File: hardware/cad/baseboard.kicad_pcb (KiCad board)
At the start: 6 copper layers, 100 x 65 mm, 129 parts, among them J201 1/4" JACK, STEREO, J202 1/4" JACK, STEREO, J301 FFC CONNECTOR, J303 2x2 PIN HEADER, J306 6-440054-2, J308 6-440054-2, J310 6-440054-2, J311 6-440054-2, J401 DC POWER JACK, J402 6-440054-2, Q301 DMN2050, Q302 DMN2050, U201 OPA1679, U202 OPA1679, U301 STM32G031K8U6, U302 ADG5434, U401 LM337, U402 LM317, U403 ADP5070, U404 LM317

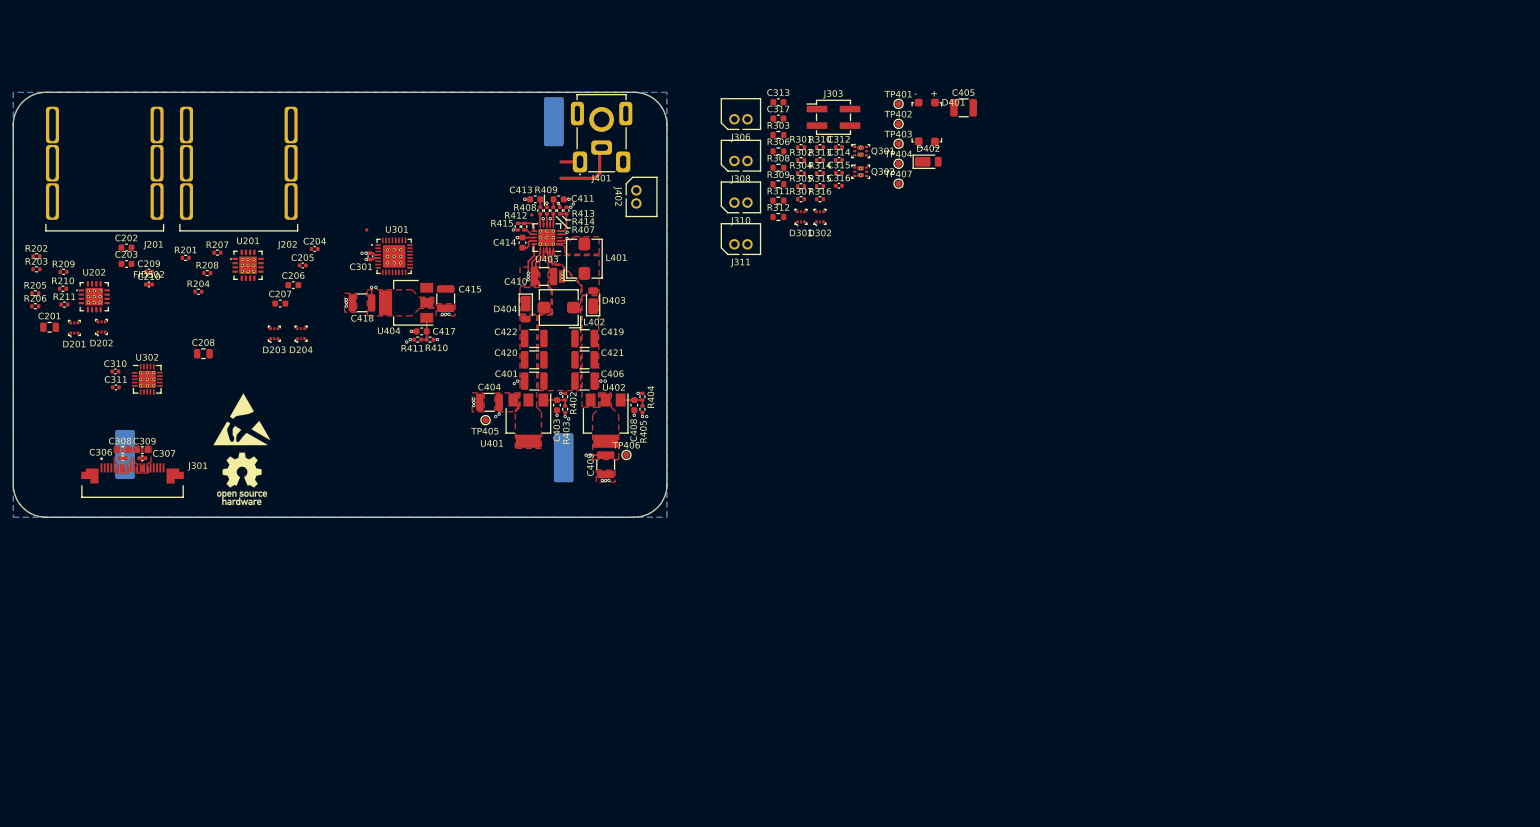
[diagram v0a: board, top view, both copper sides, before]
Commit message: finalized schematic
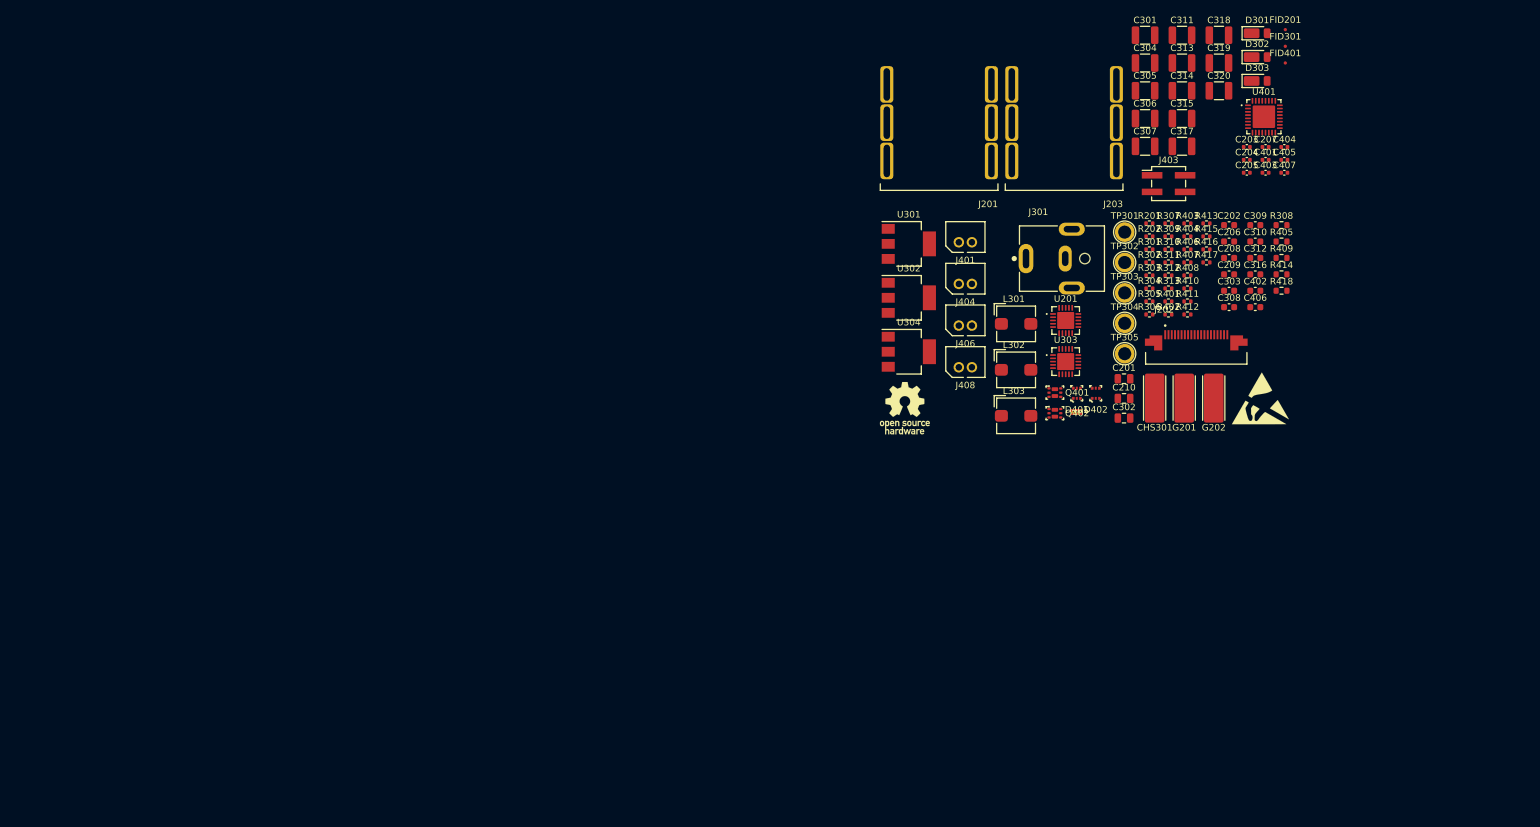
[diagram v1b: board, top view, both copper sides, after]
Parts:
- removed C408, C414, C417: 2.2µ, Capacitor_SMD:C_0603_1608Metric
- removed C409, C410, C415, C418, C419, C420, C421, C422: 22µ, Capacitor_SMD:C_1210_3225Metric
- removed C411: 2n, Capacitor_SMD:C_0603_1608Metric
- removed C413: 39n, Capacitor_SMD:C_0603_1608Metric
- removed CHS401, CHS501, CHS502: Chassis, Library:Harwin_EMI_Finger_S7061-46R
- removed D201, D202, D203, D204: RSB10JS2, Library:RSB12JS2
- removed D403, D404: DFLS240L-7, Library:D_PowerDI-123_THERMAL_PAD
- removed FID501, FID502, FID503: Fiducial, Fiducial:Fiducial_0.5mm_Mask1mm
- removed G501: OSHW LOGO, Symbol:OSHW-Logo_7.5x8mm_SilkScreen
- removed G502: ESD SYMBOL, Symbol:ESD-Logo_8.9x8mm_SilkScreen
- removed J303: 2x2 PIN HEADER, Connector_PinHeader_2.54mm:PinHeader_2x02_P2.54mm_Vertical_SMD
- removed J306, J308, J310, J311, J402: 6-440054-2, Library:TE_HPI_2.0MM_PITCH_MALE_HEADER_2POS
- removed L401, L402: 22µ, Inductor_SMD:L_Bourns_SRP5030T
- removed NT401: NetTie_2, Library:Net_Tie
- removed Q301, Q302: DMN2050, Library:DMN2050LFDB_THERMAL_VIAS
- removed R203: 1M, Resistor_SMD:R_0402_1005Metric
- removed R204, R205, R206, R207, R208, R209, R210, R211: 49.9k, Resistor_SMD:R_0402_1005Metric
- removed R314: 1k, Resistor_SMD:R_0402_1005Metric
- removed R315, R316: 120R, Resistor_SMD:R_0402_1005Metric
- removed TP401, TP402, TP403, TP404, TP405, TP406, TP407: TestPoint, TestPoint:TestPoint_Pad_D1.0mm
- removed U202: OPA1679, Library:OPA1679
- removed U402, U404: LM317, Package_TO_SOT_SMD:SOT-223-3_TabPin2
- removed U403: ADP5070, Library:LFCSP-20-1EP_4x4mm_P0.5mm_EP2.6x2.6mm_ThermalVias
- added C302: 150pF, Capacitor_SMD:C_0805_2012Metric, F.Cu at (211.4, 103.1)
- added C303: 2.2µF, Capacitor_SMD:C_0603_1608Metric, F.Cu at (227.5, 83.7)
- added C304: 10µF, Capacitor_SMD:C_1210_3225Metric, F.Cu at (214.6, 48.8)
- added C305: 10µF, Capacitor_SMD:C_1210_3225Metric, F.Cu at (214.6, 53.1)
- added C318: 10µF, Capacitor_SMD:C_1210_3225Metric, F.Cu at (225.9, 44.6)
- added C319: 10µF, Capacitor_SMD:C_1210_3225Metric, F.Cu at (225.9, 48.8)
- added C320: 10µF, Capacitor_SMD:C_1210_3225Metric, F.Cu at (225.9, 53.1)
- added C402: 2.2µF, Capacitor_SMD:C_0603_1608Metric, F.Cu at (231.5, 83.7)
- added C407: 100nF, Capacitor_SMD:C_0402_1005Metric, F.Cu at (235.9, 65.6)
- added CHS301: CHASSIS, Library:Harwin_EMI_Finger_S7061-46R, F.Cu at (216.1, 100.1)
- added D303: DFLS240L-7, Library:D_PowerDI-123_THERMAL_PAD, F.Cu at (231.8, 51.6)
- added FID201: FIDUCIAL, Fiducial:Fiducial_0.5mm_Mask1mm, F.Cu at (236.1, 43.7)
- added FID301: FIDUCIAL, Fiducial:Fiducial_0.5mm_Mask1mm, F.Cu at (236.1, 46.3)
- added FID401: FIDUCIAL, Fiducial:Fiducial_0.5mm_Mask1mm, F.Cu at (236.1, 48.8)
- added G101: OSHW LOGO, Symbol:OSHW-Logo_7.5x8mm_SilkScreen, F.Cu at (177.9, 101.6)
- added G102: ESD SYMBOL, Symbol:ESD-Logo_8.9x8mm_SilkScreen, F.Cu at (232.3, 100.1)
- added G201: CHASSIS, Library:Harwin_EMI_Finger_S7061-46R, F.Cu at (220.6, 100.1)
- added G202: CHASSIS, Library:Harwin_EMI_Finger_S7061-46R, F.Cu at (225.1, 100.1)
- added J203: 1/4" JACK, STEREO, Library:Amphenol_ACJS-IHS, F.Cu at (202.2, 58.3)
- added J403: 2x2 PIN HEADER, Connector_PinHeader_2.54mm:PinHeader_2x02_P2.54mm_Vertical_SMD, F.Cu at (218.2, 67.3)
- added J404: 6-440054-2, Library:TE_HPI_2.0MM_PITCH_MALE_HEADER_2POS, F.Cu at (187.1, 84.4)
- added J406: 6-440054-2, Library:TE_HPI_2.0MM_PITCH_MALE_HEADER_2POS, F.Cu at (187.1, 90.7)
- added J408: 6-440054-2, Library:TE_HPI_2.0MM_PITCH_MALE_HEADER_2POS, F.Cu at (187.1, 97.1)
- added L301: 22µH, Inductor_SMD:L_Bourns_SRP5030T, F.Cu at (194.9, 88.7)
- added L302: 22µH, Inductor_SMD:L_Bourns_SRP5030T, F.Cu at (194.9, 95.8)
- added L303: 22µH, Inductor_SMD:L_Bourns_SRP5030T, F.Cu at (194.9, 102.8)
- added NT301: NET TIE, Library:Net_Tie, F.Cu at (204.2, 102.2)
- added Q401: DMN2050, Library:DMN2050LFDB, F.Cu at (200.8, 99.2)
- added Q402: DMN2050, Library:DMN2050LFDB, F.Cu at (200.8, 102.4)
- added R401: 120Ω, Resistor_SMD:R_0402_1005Metric, F.Cu at (218.2, 85.3)
- added R406: 120Ω, Resistor_SMD:R_0402_1005Metric, F.Cu at (221.1, 77.3)
- added R416: 120Ω, Resistor_SMD:R_0402_1005Metric, F.Cu at (224.0, 77.3)
- added R417: 750Ω, Resistor_SMD:R_0402_1005Metric, F.Cu at (224.0, 79.3)
- added R418: 15Ω, Resistor_SMD:R_0603_1608Metric, F.Cu at (235.5, 83.7)
- added TP301: TEST POINT, TestPoint:TestPoint_Plated_Hole_D2.0mm, F.Cu at (211.5, 74.7)
- added TP302: TEST POINT, TestPoint:TestPoint_Plated_Hole_D2.0mm, F.Cu at (211.5, 79.3)
- added TP303: TEST POINT, TestPoint:TestPoint_Plated_Hole_D2.0mm, F.Cu at (211.5, 84.0)
- added TP304: TEST POINT, TestPoint:TestPoint_Plated_Hole_D2.0mm, F.Cu at (211.5, 88.6)
- added TP305: TEST POINT, TestPoint:TestPoint_Plated_Hole_D2.0mm, F.Cu at (211.5, 93.3)
- added U303: ADP5070, Library:LFCSP-20-1EP_4x4mm_P0.5mm_EP2.6x2.6mm, F.Cu at (202.5, 94.5)
- added U304: LM317, Package_TO_SOT_SMD:SOT-223-3_TabPin2, F.Cu at (178.5, 93.0)
- C201: value 150p -> 150pF
- C202: value 39n -> 39nF
- C203, C207: value 39n -> 100nF; footprint Capacitor_SMD:C_0603_1608Metric -> Capacitor_SMD:C_0402_1005Metric
- C204, C205: value 100n -> 100nF
- C206: value 39n -> 2.2µF
- C208: value 150p -> 2.2µF; footprint Capacitor_SMD:C_0805_2012Metric -> Capacitor_SMD:C_0603_1608Metric
- C209: value 100n -> 39nF; footprint Capacitor_SMD:C_0402_1005Metric -> Capacitor_SMD:C_0603_1608Metric
- C210: value 100n -> 150pF; footprint Capacitor_SMD:C_0402_1005Metric -> Capacitor_SMD:C_0805_2012Metric
- C301, C306, C307, C311, C314, C315: value 100n -> 10µF; footprint Capacitor_SMD:C_0402_1005Metric -> Capacitor_SMD:C_1210_3225Metric
- C308: value 2.2µ -> 58nF
- C309: value 2.2µ -> 2.2µF
- C310: value 100n -> 10nF; footprint Capacitor_SMD:C_0402_1005Metric -> Capacitor_SMD:C_0603_1608Metric
- C312, C316: value 100n -> 2.2µF; footprint Capacitor_SMD:C_0402_1005Metric -> Capacitor_SMD:C_0603_1608Metric
- C313, C317: value 2.2µ -> 10µF; footprint Capacitor_SMD:C_0603_1608Metric -> Capacitor_SMD:C_1210_3225Metric
- C401, C404, C405: value 22µ -> 100nF; footprint Capacitor_SMD:C_1210_3225Metric -> Capacitor_SMD:C_0402_1005Metric
- C403: value 2.2µ -> 100nF; footprint Capacitor_SMD:C_0603_1608Metric -> Capacitor_SMD:C_0402_1005Metric
- C406: value 22µ -> 2.2µF; footprint Capacitor_SMD:C_1210_3225Metric -> Capacitor_SMD:C_0603_1608Metric
- D301: value RSB10JS2 -> DFLZ13Q-7; footprint Library:RSB12JS2 -> Library:D_PowerDI-123_THERMAL_PAD
- D302: value RSB10JS2 -> DFLS240L-7; footprint Library:RSB12JS2 -> Library:D_PowerDI-123_THERMAL_PAD
- D401: value CD-HD2004 -> RSB10JS2; footprint Library:CD-HD2004L -> Library:RSB12JS2
- D402: value DFLZ13Q-7 -> RSB10JS2; footprint Library:D_PowerDI-123_THERMAL_PAD -> Library:RSB12JS2
- J202: value 1/4" JACK, STEREO -> FFC CONNECTOR; footprint Library:Amphenol_ACJS-IHS -> Library:AMPHENOL_SFV20R-2STE1HLF
- J301: value FFC CONNECTOR -> JACK, DC; footprint Library:AMPHENOL_SFV20R-2STE1HLF -> Library:CUI_PJ-063AH
- J401: value DC POWER JACK -> 6-440054-2; footprint Library:CUI_PJ-047 -> Library:TE_HPI_2.0MM_PITCH_MALE_HEADER_2POS
- R201, R310: value 49.9k -> 1MΩ
- R202: value 1M -> 49.9kΩ
- R301: value 120R -> 750Ω
- R302, R403: value 120R -> 120Ω
- R303: value 15R -> 750Ω; footprint Resistor_SMD:R_0603_1608Metric -> Resistor_SMD:R_0402_1005Metric
- R304: value 1k -> 33kΩ
- R305: value 49.9k -> 120Ω
- R306: value 15R -> 3.3kΩ; footprint Resistor_SMD:R_0603_1608Metric -> Resistor_SMD:R_0402_1005Metric
- R307, R313: value 1k -> 71.5kΩ
- R308: value 15R -> 200Ω
- R309: value 15R -> 62.5kΩ; footprint Resistor_SMD:R_0603_1608Metric -> Resistor_SMD:R_0402_1005Metric
- R311: value 15R -> 120Ω; footprint Resistor_SMD:R_0603_1608Metric -> Resistor_SMD:R_0402_1005Metric
- R312: value 15R -> 1MΩ; footprint Resistor_SMD:R_0603_1608Metric -> Resistor_SMD:R_0402_1005Metric
- R402: value 750R -> 49.9kΩ
- R404: value 750R -> 750Ω
- R405: value 120R -> 200Ω; footprint Resistor_SMD:R_0402_1005Metric -> Resistor_SMD:R_0603_1608Metric
- R407: value 18k -> 120Ω
- R408: value 1.8k -> 750Ω
- R409: value 100k -> 15Ω; footprint Resistor_SMD:R_0402_1005Metric -> Resistor_SMD:R_0603_1608Metric
- R410: value 200R -> 120Ω
- R411: value 120R -> 49.9kΩ
- R412: value 71.5k -> 120Ω
- R413: value 1.4M -> 750Ω
- R414: value 100k -> 200Ω; footprint Resistor_SMD:R_0402_1005Metric -> Resistor_SMD:R_0603_1608Metric
- R415: value 1.15M -> 120Ω
- U201: value OPA1679 -> ADG5434; footprint Library:OPA1679 -> Library:LFCSP-20-1EP_4x4mm_P0.5mm_EP2.6x2.6mm
- U301: value STM32G031K8U6 -> LM337; footprint Library:QFN-32-1EP_5x5mm_P0.5mm_EP3.45x3.45mm_ThermalVias -> Package_TO_SOT_SMD:SOT-223-3_TabPin2
- U302: value ADG5434 -> LM317; footprint Library:LFCSP-20-1EP_4x4mm_P0.5mm_EP2.6x2.6mm_ThermalVias -> Package_TO_SOT_SMD:SOT-223-3_TabPin2
- U401: value LM337 -> STM32G031K8U6; footprint Package_TO_SOT_SMD:SOT-223-3_TabPin2 -> Library:QFN-32-1EP_5x5mm_P0.5mm_EP3.45x3.45mm
- moved C310 175.5 mm to (231.5, 76.1)
- moved C309 173.7 mm to (231.5, 73.6), turned to 0 degrees
- moved C203 172.3 mm to (230.2, 61.7)
- moved C311 171.7 mm to (220.3, 44.6)
- moved C308 170.6 mm to (227.5, 86.2)
- moved R202 170.3 mm to (215.3, 75.3)
- moved C202 168.7 mm to (227.5, 73.6)
- moved C209 165.2 mm to (227.5, 81.1)
- moved C306 164.8 mm to (214.6, 57.3)
- moved C201 164.5 mm to (211.4, 97.1)
- moved C307 160.6 mm to (214.6, 61.6), turned to 0 degrees
- moved C208 157.6 mm to (227.5, 78.6)
- moved C207 152.6 mm to (233.1, 61.7)
- moved C210 150.2 mm to (211.4, 100.1)
- moved J202 149.2 mm to (222.5, 92.8)
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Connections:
- C201 pad 1: /Input and Output/AUDIO_IN+ -> /AUDIO/AUDIO_IN-
- C201 pad 2: /Input and Output/AUDIO_IN- -> GND
- C202 pad 1: AUDIO_IN_FILT+ -> AUDIO_IN_FILT
- C202 pad 2: /Input and Output/AUDIO_IN+ -> /AUDIO/AUDIO_IN-
- C203 pad 1: AUDIO_IN_FILT- -> GND
- C203 pad 2: /Input and Output/AUDIO_IN- -> +9V
- C204 pad 1: GND -> -9V
- C204 pad 2: +9V -> GND
- C205 pad 1: -9V -> GND
- C205 pad 2: GND -> +9V
- C206 pad 1: /Input and Output/AUDIO_OUT+ -> GND
- C206 pad 2: AUDIO_OUT_FILT+ -> +9V
- C207 pad 1: /Input and Output/AUDIO_OUT- -> GND
- C207 pad 2: AUDIO_OUT_FILT- -> -9V
- C208 pad 1: /Input and Output/AUDIO_OUT+ -> GND
- C208 pad 2: /Input and Output/AUDIO_OUT- -> -9V
- C209 pad 1: GND -> /AUDIO/AUDIO_OUT
- C209 pad 2: +9V -> AUDIO_OUT_FILT
- C210 pad 1: -9V -> /AUDIO/AUDIO_OUT
- C301 pad 2: +3V3 -> -12V_RAW
- C306 pad 2: +9V -> +12V_RAW
- C307 pad 1: GND -> GND1
- C307 pad 2: -9V -> DC_IN
- C308 pad 2: +9V -> Net-(C308-Pad2)
- C309 pad 2: -9V -> /POWER/+9VREG_FBP
- C310 pad 2: +9V -> Net-(C310-Pad2)
- C311 pad 1: -9V -> GND
- C311 pad 2: GND -> +9V
- C312 pad 2: +3V3 -> /POWER/VSW_VREG
- C313 pad 2: /Microcontroller and Switching/V_FTSW_FILT_A -> DC_IN
- C314 pad 1: GND -> Net-(D303-A)
- C314 pad 2: +3V3 -> Net-(U303-SW1)
- C315 pad 1: GND -> GND1
- C315 pad 2: +3V3 -> -12V_RAW
- C316 pad 2: +3V3 -> /POWER/3V3REG_FB
- C317 pad 1: GND -> GND1
- C317 pad 2: /Microcontroller and Switching/V_FTSW_FILT_B -> -12V_RAW
- C401 pad 1: GND1 -> GND
- C401 pad 2: -12V_RAW -> +3V3
- C403 pad 2: /Power/-9VREG_FBN -> +3V3
- C404 pad 2: -9V -> +3V3
- C405 pad 2: DC_IN -> +3V3
- C406 pad 1: GND1 -> GND
- C406 pad 2: +12V_RAW -> /MICROCONTROLLER/V_FTSW_FILT_A
- D301 pad 1: +3V3 -> DC_IN
- D301 pad 2: /Microcontroller and Switching/SWDIO -> GND
- D302 pad 1: +3V3 -> /POWER/VSW2
- D302 pad 2: /Microcontroller and Switching/SWDCK -> -12V_RAW
- D401 pad 1: /Power/DC_IN- -> +3V3
- D401 pad 2: /Power/DC_IN+ -> /MICROCONTROLLER/SWDIO
- D401 pad 3: DC_IN -> (no net)
- D402 pad 1: DC_IN -> +3V3
- D402 pad 2: GND -> /MICROCONTROLLER/SWDCK
- J201 pad R: BATT_SW- -> GND
- J201 pad S: /Input and Output/AUDIO_IN+ -> GND
- J201 pad T: /Input and Output/AUDIO_IN- -> /AUDIO/AUDIO_IN-
- J301 pad 2: AUDIO_IN_A -> DC_IN
- J401 pad 1: /Power/DC_IN- -> /MICROCONTROLLER/V_FTSW_RAW_B
- J401 pad 2: /Power/DC_IN+ -> +3V3
- R201 pad 1: /Input and Output/AUDIO_OUT_SE_BUFFER -> /AUDIO/AUDIO_IN-
- R201 pad 2: /Input and Output/SE-DIFF_INV_FB -> GND
- R202 pad 1: /Input and Output/AUDIO_IN+ -> /AUDIO/AUDIO_OUT
- R301 pad 1: /Microcontroller and Switching/V_FTSW_FILT_A -> /POWER/-9VREG_FBN
- R301 pad 2: Net-(Q301A-G) -> GND
- R302 pad 1: /Microcontroller and Switching/V_FTSW_FILT_B -> -9V
- R302 pad 2: Net-(Q302A-G) -> /POWER/-9VREG_FBN
- R303 pad 1: /Microcontroller and Switching/V_FTSW_RAW_A -> /POWER/+9VREG_FBP
- R303 pad 2: /Microcontroller and Switching/V_FTSW_FILT_A -> GND
- R304 pad 1: GND -> Net-(C308-Pad2)
- R304 pad 2: Net-(Q301B-G) -> /POWER/VSW_COMP1
- R305 pad 1: GND -> +9V
- R305 pad 2: /Microcontroller and Switching/V_FTSW_FILT_A -> /POWER/+9VREG_FBP
- R306 pad 1: /Microcontroller and Switching/V_LEDA -> Net-(C310-Pad2)
- R306 pad 2: /Microcontroller and Switching/VS_A -> /POWER/VSW_COMP2
- R307 pad 2: Net-(Q302B-G) -> /POWER/VSW_SOFT_START
- R308 pad 1: /Microcontroller and Switching/V_FTSW_RAW_B -> /POWER/3V3REG_FB
- R308 pad 2: /Microcontroller and Switching/V_FTSW_FILT_B -> GND
- R309 pad 1: /Microcontroller and Switching/V_LEDB -> /POWER/VSW_FB2
- R309 pad 2: /Microcontroller and Switching/VS_B -> /POWER/VSW_VREF
- R310 pad 1: GND -> -12V_RAW
- R310 pad 2: /Microcontroller and Switching/V_FTSW_FILT_B -> /POWER/VSW_FB2
- R311 pad 2: FTSW_A -> /POWER/3V3REG_FB
- R312 pad 1: +3V3 -> /POWER/VSW_FB1
- R312 pad 2: FTSW_B -> +12V_RAW
- R313 pad 2: Net-(Q301A-G) -> /POWER/VSW_FB1
- R402 pad 1: /Power/-9VREG_FBN -> GND
- R402 pad 2: GND -> /MICROCONTROLLER/V_FTSW_FILT_B
- R403 pad 1: -9V -> /MICROCONTROLLER/V_FTSW_FILT_B
- R403 pad 2: /Power/-9VREG_FBN -> Net-(Q401A-G)
- R404 pad 1: /Power/+9VREG_FBP -> Net-(Q401A-G)
- R405 pad 1: +9V -> +3V3
- R405 pad 2: /Power/+9VREG_FBP -> Net-(Q401A-D)
- R407 pad 1: Net-(C411-Pad2) -> LEDB_EN
- R407 pad 2: /Power/VSW_COMP1 -> Net-(Q401B-G)
- R408 pad 1: Net-(C413-Pad2) -> Net-(Q401B-G)
- R408 pad 2: /Power/VSW_COMP2 -> GND
- R409 pad 1: GND -> /MICROCONTROLLER/V_LEDB
- R409 pad 2: /Power/VSW_SOFT_START -> /MICROCONTROLLER/VS_B
- R410 pad 1: /Power/3V3REG_FB -> /MICROCONTROLLER/V_FTSW_RAW_A
- R410 pad 2: GND -> /MICROCONTROLLER/V_FTSW_FILT_A
- R411 pad 1: +3V3 -> GND
- R411 pad 2: /Power/3V3REG_FB -> /MICROCONTROLLER/V_FTSW_FILT_A
- R412 pad 1: /Power/VSW_FB2 -> /MICROCONTROLLER/V_FTSW_FILT_A
- R412 pad 2: /Power/VSW_VREF -> Net-(Q402A-G)
- R413 pad 1: /Power/VSW_FB1 -> Net-(Q402A-G)
- R413 pad 2: +12V_RAW -> GND
- R414 pad 1: GND -> +3V3
- R414 pad 2: /Power/VSW_FB1 -> Net-(Q402A-D)
- R415 pad 1: -12V_RAW -> Net-(Q402A-D)
- R415 pad 2: /Power/VSW_FB2 -> FTSW_A
- U201 pad 1: AUDIO_OUT_FILT- -> AUDIO_IN_FILT
- U201 pad 10: -9V -> AUDIO_IN_B
- U201 pad 11: AUDIO_OUT_SE -> /AUDIO/AUDIO_A_TO_B
- U201 pad 12: AUDIO_OUT_FILT+ -> /AUDIO/BYPASS_B
- U201 pad 13: unconnected-(U201E-NC-Pad13) -> +9V
- U201 pad 14: AUDIO_OUT_FILT+ -> AUDIO_OUT_B
- U201 pad 15: AUDIO_OUT_FILT- -> AUDIO_OUT_FILT
- U201 pad 16: unconnected-(U201E-NC-Pad16) -> /AUDIO/BYPASS_B
- U201 pad 17: GND -> SW_IN4
- U201 pad 2: /Input and Output/SE-DIFF_INV_OUT -> /AUDIO/BYPASS_A
- U201 pad 3: +9V -> -9V
- U201 pad 5: /Input and Output/SE-DIFF_INV_FB -> AUDIO_OUT_A
- U201 pad 6: /Input and Output/SE-DIFF_INV_OUT -> /AUDIO/AUDIO_A_TO_B
- U201 pad 7: /Input and Output/AUDIO_OUT_SE_BUFFER -> /AUDIO/BYPASS_A
- U201 pad 8: /Input and Output/AUDIO_OUT_SE_BUFFER -> SW_IN2
- U201 pad 9: AUDIO_OUT_SE -> SW_IN3
- U301 pad 1: unconnected-(U301-PB9-Pad1) -> /POWER/-9VREG_FBN
- U301 pad 2: FTSW_A -> -12V_RAW
- U301 pad 3: FTSW_B -> -9V
- U302 pad 1: AUDIO_IN_SE -> /POWER/+9VREG_FBP
- U302 pad 2: /Microcontroller and Switching/BYPASS_A -> +9V
- U302 pad 3: -9V -> +12V_RAW
- U401 pad 1: /Power/-9VREG_FBN -> unconnected-(U401-PB9-Pad1)
- U401 pad 2: -12V_RAW -> FTSW_A
- U401 pad 3: -9V -> LEDA_EN
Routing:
- net +12V_RAW: track 30.2 -> 0.00 mm, vias 2 -> 0
- net -12V_RAW: track 25.1 -> 0.00 mm, vias 2 -> 0
- net +9V: track 15.9 -> 0.00 mm, vias 11 -> 0
- net +3V3: track 15.3 -> 0.00 mm, vias 3 -> 0
- net DC_IN: track 14.7 -> 0.00 mm, vias 3 -> 0
- net GND: track 14.5 -> 0.00 mm, vias 27 -> 0
- net -9V: track 13.1 -> 0.00 mm, vias 2 -> 0
- net /Power/DC_IN+: track 10.3 -> 0.00 mm
- net /Power/VSW_FB1: track 4.43 -> 0.00 mm
- net /Power/-9VREG_FBN: track 4.22 -> 0.00 mm
- net /Power/+9VREG_FBP: track 4.22 -> 0.00 mm
- net /Power/3V3REG_FB: track 4.20 -> 0.00 mm
- net /Power/VSW_FB2: track 3.46 -> 0.00 mm
- net /Power/DC_IN-: track 2.92 -> 0.00 mm
- net /Power/VSW_VREG: track 2.59 -> 0.00 mm
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- removed copper zone on F.Cu, net +12V_RAW
- removed copper zone on F.Cu, net +3V3
- removed copper zone on F.Cu, net +9V
- removed copper zone on F.Cu, net -12V_RAW
- removed copper zone on F.Cu, net -9V
- removed copper zone on F.Cu, net /Power/VSW1
- removed copper zone on F.Cu, net /Power/VSW2
- removed copper zone on F.Cu, net DC_IN
- removed copper zone on In2.Cu, net DC_IN
- removed copper zone on B.Cu, net GND
- removed copper zone on F.Cu, net GND
- removed copper zone on In1.Cu, net GND
- removed copper zone on In2.Cu, net GND
- removed copper zone on In3.Cu, net GND
- removed copper zone on In4.Cu, net GND
- removed copper zone on F.Cu, net GND1
- removed copper zone on F.Cu, net Net-(D403-A)
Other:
- board outline removed
- board text removed: "INITIAL RELEASE"

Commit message: board layout first pass
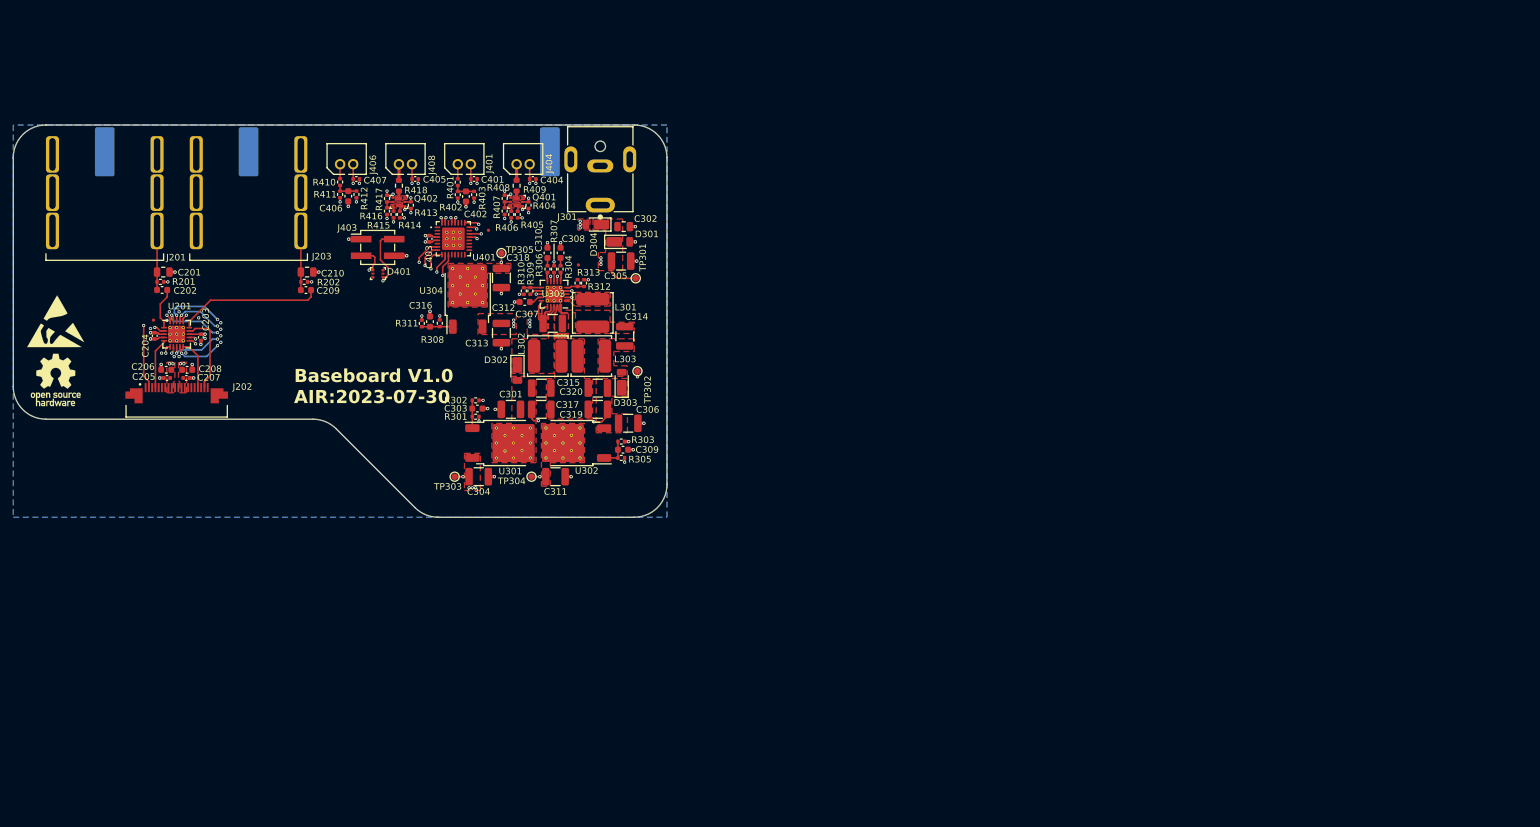
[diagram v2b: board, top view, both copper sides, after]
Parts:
- removed CHS301: CHASSIS, Library:Harwin_EMI_Finger_S7061-46R
- removed D402: RSB10JS2, Library:RSB12JS2
- added D304: DFLS240L-7, Library:D_PowerDI-123_THERMAL_PAD, F.Cu at (130.6, 73.5)
- added G301: CHASSIS, Library:Harwin_EMI_Finger_S7061-46R, B.Cu at (123.6, 62.4)
- C206, C208, C303, C309, C312, C316, C402, C406: value 2.2µF -> 2.2μF
- C301, C304, C305, C306, C307, C311, C313, C314, C315, C317, C318, C319, C320: value 10µF -> 10μF
- D401: value RSB10JS2 -> TVS
- G201, G202: moved to B.Cu
- L301, L302, L303: value 22µH -> 22μH; footprint Inductor_SMD:L_Bourns_SRP5030T -> Library:L_TDK_VLS6045EX_VLS6045AF
- R308, R405, R414: footprint Resistor_SMD:R_0603_1608Metric -> Resistor_SMD:R_0402_1005Metric
- TP301, TP302, TP303, TP304, TP305: footprint TestPoint:TestPoint_Plated_Hole_D2.0mm -> TestPoint:TestPoint_Pad_D1.0mm
- U201, U303: footprint Library:LFCSP-20-1EP_4x4mm_P0.5mm_EP2.6x2.6mm -> Library:LFCSP-20-1EP_4x4mm_P0.5mm_EP2.6x2.6mm_ThermalVias
- U301, U302, U304: footprint Package_TO_SOT_SMD:SOT-223-3_TabPin2 -> Library:TO-252-2_THERMAL_PAD
- U401: footprint Library:QFN-32-1EP_5x5mm_P0.5mm_EP3.45x3.45mm -> Library:QFN-32-1EP_5x5mm_P0.5mm_EP3.45x3.45mm_ThermalVias
- moved G102 184.7 mm to (48.0, 88.3)
- moved FID201 178.7 mm to (63.0, 88.2)
- moved G201 169.4 mm to (55.5, 62.4), turned to 180 degrees
- moved C204 169.2 mm to (63.1, 90.5), turned to -90 degrees
- moved C207 168.8 mm to (68.0, 97.0), turned to 180 degrees
- moved C205 168.1 mm to (65.0, 97.0)
- moved C206 163.8 mm to (64.9, 95.8)
- moved C202 163.5 mm to (64.3, 83.5), turned to 180 degrees
- moved C203 162.6 mm to (70.2, 90.8), turned to 90 degrees
- moved C208 160.3 mm to (68.1, 95.8), turned to 180 degrees
- moved J202 156.2 mm to (66.5, 100.9)
- moved G202 152.4 mm to (77.5, 62.4), turned to 180 degrees
- moved R201 151.5 mm to (64.0, 82.3)
- moved C201 147.9 mm to (64.5, 80.8)
- moved C407 142.0 mm to (94.0, 66.6), turned to 180 degrees
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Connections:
- net /POWER/VSW1 renamed /POWER/VSW1INBK
- net Net-(D303-A) renamed /POWER/VSW1B
- net Net-(Q401A-D) renamed /MICROCONTROLLER/VD_FTSW_B
- net Net-(Q401A-G) renamed /MICROCONTROLLER/VG_FTSW_B
- net Net-(Q401B-G) renamed /MICROCONTROLLER/VG_LEDB
- net Net-(Q402A-D) renamed /MICROCONTROLLER/VD_FTSW_A
- net Net-(Q402A-G) renamed /MICROCONTROLLER/VG_FTSW_A
- net Net-(Q402B-G) renamed /MICROCONTROLLER/VG_LEDA
- net Net-(U303-SW1) renamed /POWER/VSW1A
- D401 pad 1: +3V3 -> /MICROCONTROLLER/SWDIO
- D401 pad 2: /MICROCONTROLLER/SWDIO -> GND
- D401 pad 4: GND -> /MICROCONTROLLER/SWDCK
- D401 pad 5: /MICROCONTROLLER/SWDIO -> GND
- J301 pad 2: DC_IN -> /POWER/DC_IN_RAW
- L303 pad 1: GND -> GND1
- U401 pad 10: unconnected-(U401-PA3-Pad10) -> SW_IN2
- U401 pad 11: unconnected-(U401-PA4-Pad11) -> SW_IN3
- U401 pad 15: +9V_EN -> unconnected-(U401-PB0-Pad15)
- U401 pad 16: -9V_EN -> unconnected-(U401-PB1-Pad16)
- U401 pad 18: SW_IN2 -> unconnected-(U401-PA8-Pad18)
- U401 pad 19: SW_IN3 -> unconnected-(U401-PA9/NC-Pad19)
- U401 pad 2: FTSW_A -> unconnected-(U401-PC14-Pad2)
- U401 pad 21: SW_IN1 -> -9V_EN
- U401 pad 22: SW_EN -> +9V_EN
- U401 pad 23: SW_IN4 -> unconnected-(U401-PA12/PA10-Pad23)
- U401 pad 27: FTSW_B -> unconnected-(U401-PB3-Pad27)
- U401 pad 28: LEDB_EN -> FTSW_B
- U401 pad 29: unconnected-(U401-PB5-Pad29) -> LEDB_EN
- U401 pad 3: LEDA_EN -> unconnected-(U401-PC15-Pad3)
- U401 pad 31: unconnected-(U401-PB7-Pad31) -> FTSW_A
- U401 pad 32: unconnected-(U401-PB8-Pad32) -> LEDA_EN
- U401 pad 7: unconnected-(U401-PA0-Pad7) -> SW_EN
- U401 pad 8: unconnected-(U401-PA1-Pad8) -> SW_IN4
- U401 pad 9: unconnected-(U401-PA2-Pad9) -> SW_IN1
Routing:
- net SW_IN3: track 0.00 -> 49.9 mm, vias 0 -> 3
- net SW_IN1: track 0.00 -> 49.8 mm, vias 0 -> 3
- net SW_IN2: track 0.00 -> 49.1 mm, vias 0 -> 3
- net SW_EN: track 0.00 -> 48.3 mm, vias 0 -> 3
- net SW_IN4: track 0.00 -> 46.9 mm, vias 0 -> 3
- net GND: track 0.00 -> 40.7 mm, vias 0 -> 64
- net +3V3: track 0.00 -> 39.8 mm, vias 0 -> 10
- net /MICROCONTROLLER/SWDIO: track 0.00 -> 29.9 mm, vias 0 -> 2
- net /MICROCONTROLLER/SWDCK: track 0.00 -> 26.7 mm, vias 0 -> 2
- net +12V_RAW: track 0.00 -> 26.2 mm, vias 0 -> 2
- net -12V_RAW: track 0.00 -> 23.8 mm, vias 0 -> 2
- net AUDIO_OUT_FILT: track 0.00 -> 22.2 mm
- net +9V: track 0.00 -> 19.2 mm, vias 0 -> 5
- net -9V: track 0.00 -> 17.9 mm, vias 0 -> 8
- net +9V_EN: track 0.00 -> 17.0 mm, vias 0 -> 2
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- added copper zone on F.Cu, net +12V_RAW
- added copper zone on F.Cu, net +3V3
- added copper zone on In4.Cu, net +3V3
- added copper zone on F.Cu, net +9V
- added copper zone on In4.Cu, net +9V
- added copper zone on F.Cu, net -12V_RAW
- added copper zone on F.Cu, net -9V
- added copper zone on In4.Cu, net -9V
- added copper zone on F.Cu, net /MICROCONTROLLER/VD_FTSW_A
- added copper zone on F.Cu, net /MICROCONTROLLER/VD_FTSW_B
- added copper zone on F.Cu, net /MICROCONTROLLER/VS_A
- added copper zone on F.Cu, net /MICROCONTROLLER/VS_B
- added copper zone on F.Cu, net /POWER/DC_IN_RAW
- added copper zone on In4.Cu, net /POWER/DC_IN_RAW
- added copper zone on F.Cu, net /POWER/VSW1A
- added copper zone on F.Cu, net /POWER/VSW1B
- added copper zone on F.Cu, net /POWER/VSW1INBK
- added copper zone on F.Cu, net /POWER/VSW2
- added copper zone on F.Cu, net DC_IN
- added copper zone on In4.Cu, net DC_IN
- added copper zone on B.Cu, net GND
- added copper zone on In1.Cu, net GND
- added copper zone on In3.Cu, net GND
- added copper zone on F.Cu, net GND1
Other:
- board outline added: 100 x 60 mm
- board text added: "Baseboard V1.0 AIR:2023-07-30"
